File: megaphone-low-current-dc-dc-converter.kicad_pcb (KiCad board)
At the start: 4 copper layers, 38.7 x 60 mm, 53 parts, among them Q1 SI7272DP, Q3 2N7002, U2 AP63203WU, U3 ACS712-20A, U4 ACS712-20A, U5 MCP4018

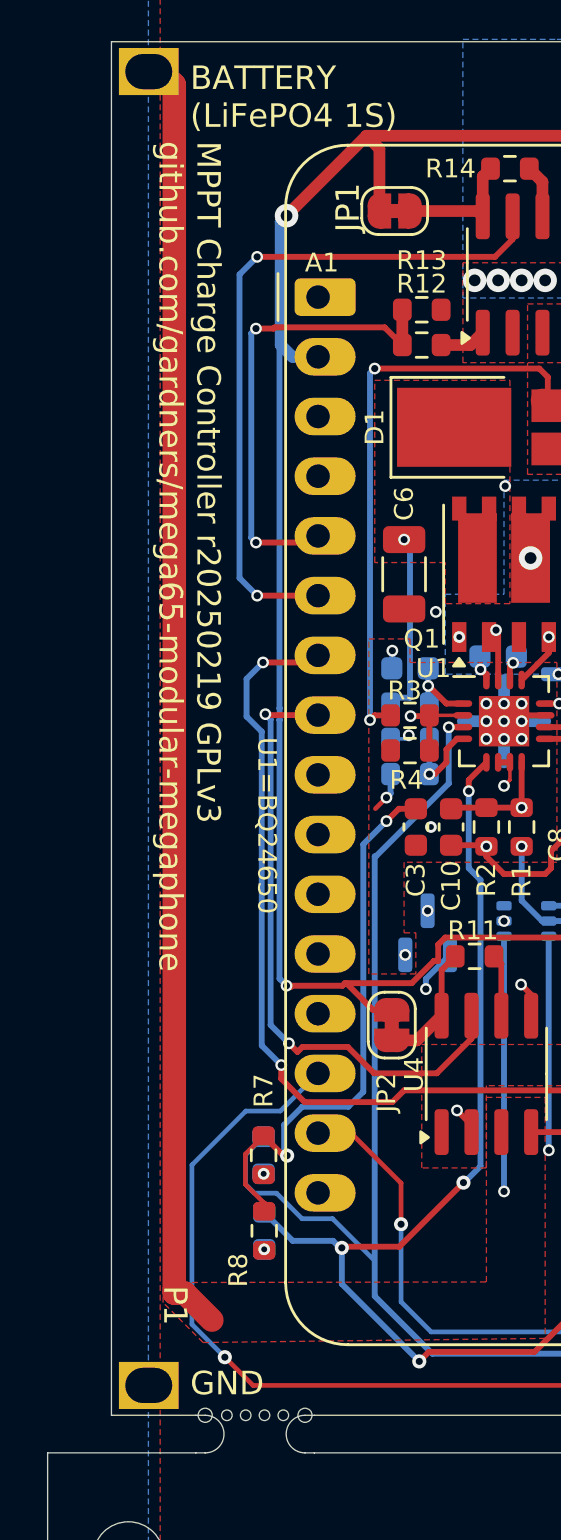
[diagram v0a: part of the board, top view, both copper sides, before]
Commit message: change all MPPT references in files to new project name
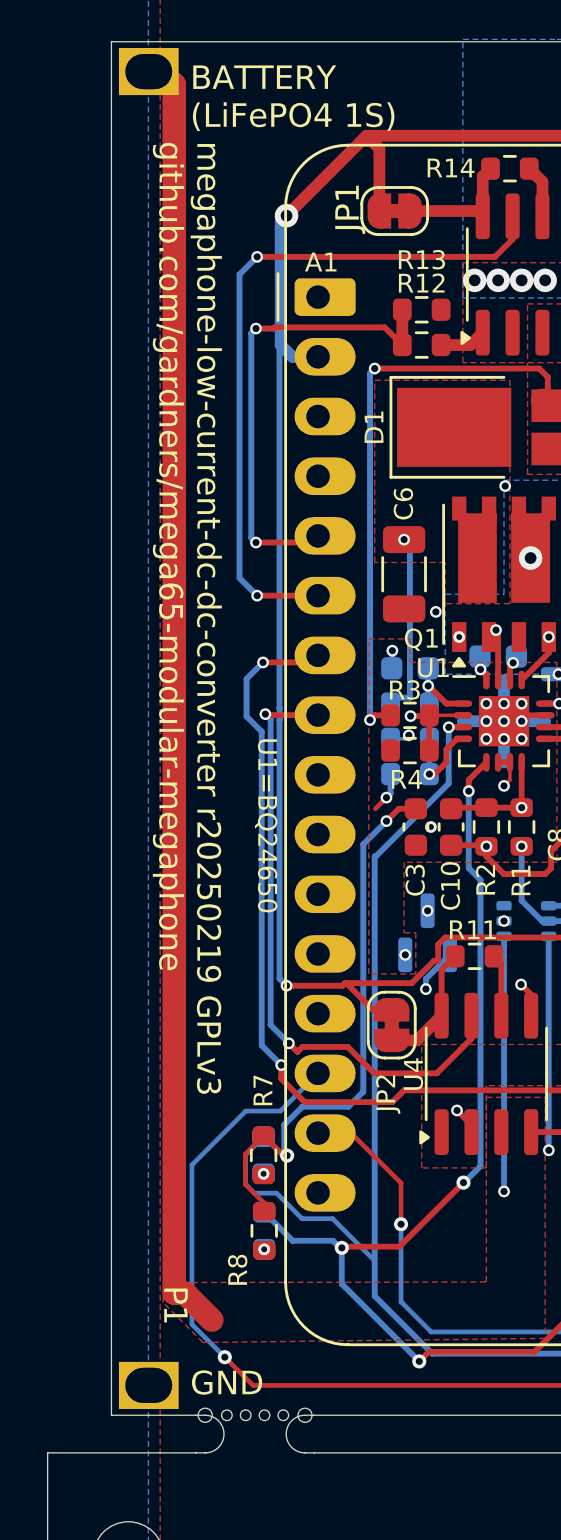
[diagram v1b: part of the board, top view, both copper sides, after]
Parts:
- L1: footprint MPPT Charge Controller Footprint Library:L_Vishay_6.9x6.5 -> megaphone-low-current-dc-dc-converter Footprint Library:L_Vishay_6.9x6.5
- U1: footprint MPPT Charge Controller Footprint Library:VQFN-16_EP_3.5x3.5_Pitch0.5mm -> megaphone-low-current-dc-dc-converter Footprint Library:VQFN-16_EP_3.5x3.5_Pitch0.5mm

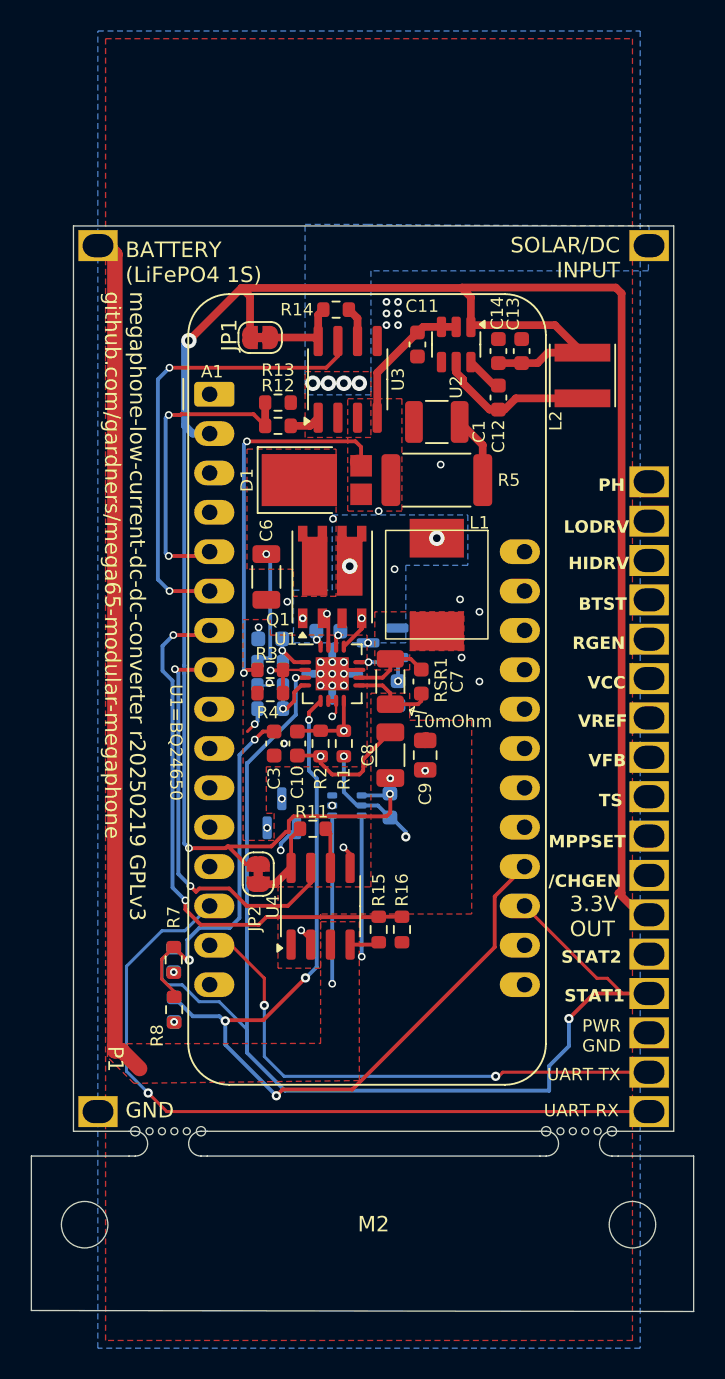
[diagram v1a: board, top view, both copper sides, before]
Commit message: prune out unnecessary part of schematic
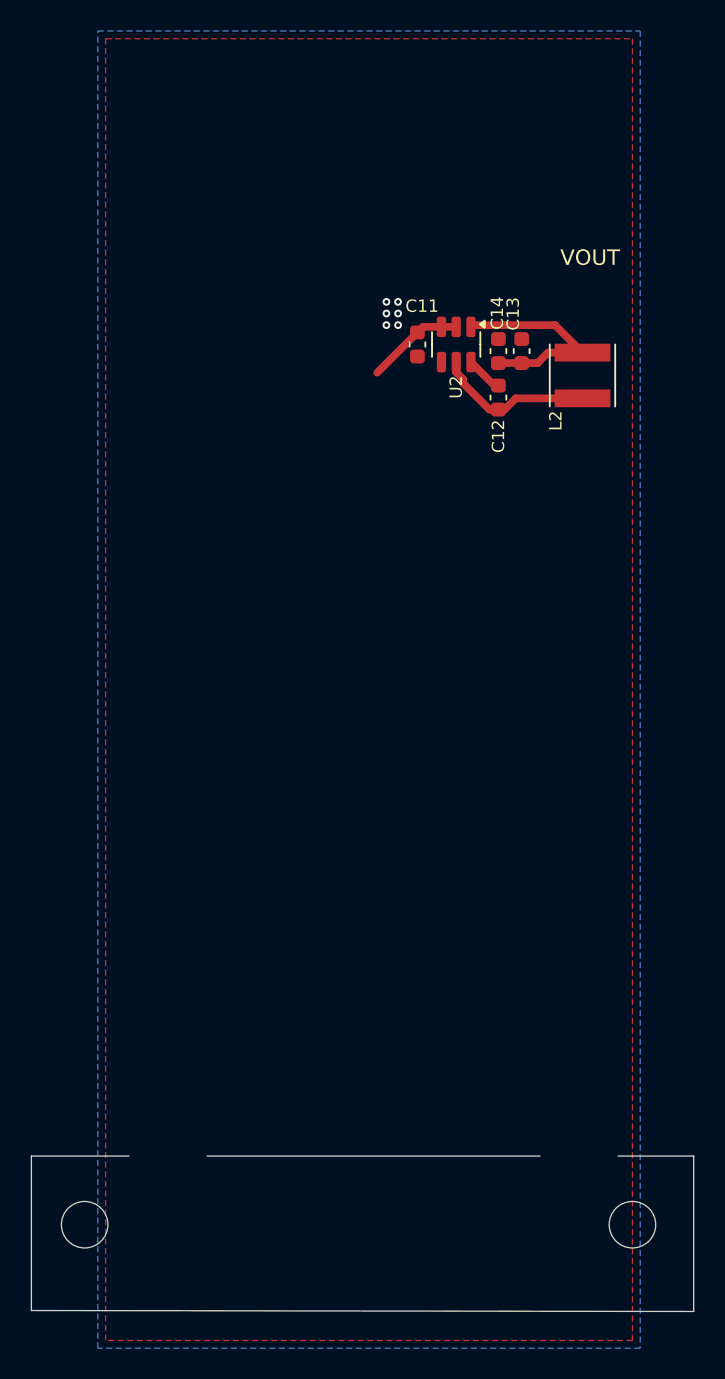
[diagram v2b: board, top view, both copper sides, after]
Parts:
- removed A1: Adafruit_Feather_HUZZAH32_ESP32, Module:Adafruit_Feather
- removed C1: 2.2uF, Capacitor_SMD:C_1210_3225Metric
- removed C10: 22pF, Capacitor_SMD:C_0603_1608Metric
- removed C15, C5, C7: 0.1uF, Capacitor_SMD:C_0603_1608Metric
- removed C2: C2=1uF, Capacitor_SMD:C_0603_1608Metric
- removed C3, C4: 1uF, Capacitor_SMD:C_0603_1608Metric
- removed C6, C8: 10uF, Capacitor_SMD:C_1206_3216Metric
- removed C9: 4.7uF, Capacitor_SMD:C_0805_2012Metric
- removed D1: PDS1040, Diode_SMD:D_PowerDI-5
- removed D2: BAT54C, Package_TO_SOT_SMD:SOT-23
- removed D3: RED, LED_SMD:LED_0603_1608Metric
- removed D4: GREEN, LED_SMD:LED_0603_1608Metric
- removed JP1, JP2: Jumper_2_Bridged, Jumper:SolderJumper-2_P1.3mm_Bridged_RoundedPad1.0x1.5mm
- removed L1: 10uH, megaphone-low-current-dc-dc-converter Footprint Library:L_Vishay_6.9x6.5
- removed M2: ~, MegaCastle:MegaCastle2x23-Module-I30.0x53.6-M80000307FFFC-PANEL-NIBBLE
- removed NT1, NT2, NT3, NT4: ~, NetTie:NetTie-2_SMD_Pad0.5mm
- removed Q1: SI7272DP, Package_SO:PowerPAK_SO-8_Dual
- removed Q3: 2N7002, Package_TO_SOT_SMD:SOT-23
- removed R1, R11, R14, R16: 100k, Resistor_SMD:R_0603_1608Metric
- removed R10: R10=30.1k, Resistor_SMD:R_0603_1608Metric
- removed R12, R15, R3: 499k, Resistor_SMD:R_0603_1608Metric
- removed R13: 36k, Resistor_SMD:R_0603_1608Metric
- removed R2: 140K, Resistor_SMD:R_0603_1608Metric
- removed R4: DNP, Resistor_SMD:R_0603_1608Metric
- removed R5: 2 Ohm, Resistor_SMD:R_2512_6332Metric
- removed R6: R6=10, Resistor_SMD:R_0603_1608Metric
- removed R7, R8: 100, Resistor_SMD:R_0603_1608Metric
- removed R9: R9=5.23k, Resistor_SMD:R_0603_1608Metric
- removed RSR1: 10mOhm, Resistor_SMD:R_1206_3216Metric
- removed U1: ~, megaphone-low-current-dc-dc-converter Footprint Library:VQFN-16_EP_3.5x3.5_Pitch0.5mm
- removed U3, U4: ACS712-20A, Package_SO:SOIC-8_3.9x4.9mm_P1.27mm
- removed U5: MCP4018, Package_TO_SOT_SMD:SOT-363_SC-70-6
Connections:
- net +3.3V renamed VOUT
- C11 pad 2: /VIN -> VBAT
- U2 pad 2: /VIN -> EN
- U2 pad 3: /VIN -> VBAT
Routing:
- net VOUT: track 146.3 -> 14.2 mm, vias 3 -> 0
- net /STAT1: track 79.1 -> 0.00 mm, vias 2 -> 0
- net /STAT2: track 69.8 -> 0.00 mm, vias 4 -> 0
- net VBAT_OUT: track 56.7 -> 0.00 mm
- net UART_RX: track 48.6 -> 0.00 mm, vias 1 -> 0
- net /VREF: track 48.5 -> 0.00 mm, vias 4 -> 0
- net /MPPSET: track 37.4 -> 0.00 mm, vias 3 -> 0
- net /Battery Voltage: track 35.7 -> 0.00 mm, vias 2 -> 0
- net UART_TX: track 34.9 -> 0.00 mm, vias 2 -> 0
- net /VCC: track 34.8 -> 0.00 mm, vias 4 -> 0
- net /VIN: track 34.3 -> 0.00 mm, vias 2 -> 0
- net PWR_GND: track 32.7 -> 0.00 mm, vias 14 -> 0
- net /TS: track 31.1 -> 0.00 mm, vias 2 -> 0
- net /HIDRV: track 30.0 -> 0.00 mm, vias 2 -> 0
- net /Solar Current: track 29.8 -> 0.00 mm, vias 2 -> 0
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- removed copper zone on B.Cu, net /Input
- removed copper zone on F.Cu, net /Input
- removed copper zone on B.Cu, net /PH
- removed copper zone on F.Cu, net /VIN
- removed copper zone on In1.Cu, net /VREF
- removed copper zone on F.Cu, net Net-(D1-K)
- removed copper zone on F.Cu, net Net-(U1-SRN)
- removed copper zone on F.Cu, net Net-(U1-SRP)
- removed copper zone on B.Cu, net PWR_GND
- removed copper zone on F.Cu, net PWR_GND
- removed copper zone on F.Cu, net VBAT_OUT
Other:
- board size 38.7 x 60 mm -> 42.7 x 10 mm
- board text added: "VOUT"
- board text removed: "${TITLE} r20250219 GPLv3 github.com/gardners/mega65-modular-megaphone"
- board text removed: "/CHGEN"
- board text removed: "3.3V OUT"
- board text removed: "BATTERY (LiFePO4 1S)"
- board text removed: "BTST"
- board text removed: "Charging"
- board text removed: "Done"
- board text removed: "GND"
- board text removed: "HIDRV"
- board text removed: "LODRV"
- board text removed: "MPPSET"
- board text removed: "P1"
- board text removed: "PH"
- board text removed: "PWR GND"
- board text removed: "RGEN"
- board text removed: "SOLAR/DC INPUT"
- board text removed: "STAT1"
- board text removed: "STAT2"
- board text removed: "TS"
- board text removed: "U1=BQ24650"
- board text removed: "UART RX"
- board text removed: "UART TX"
- board text removed: "VCC"
- board text removed: "VFB"
- board text removed: "VREF"

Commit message: finish adapting MPPT into simple low-current 3.3V DC:DC regulator
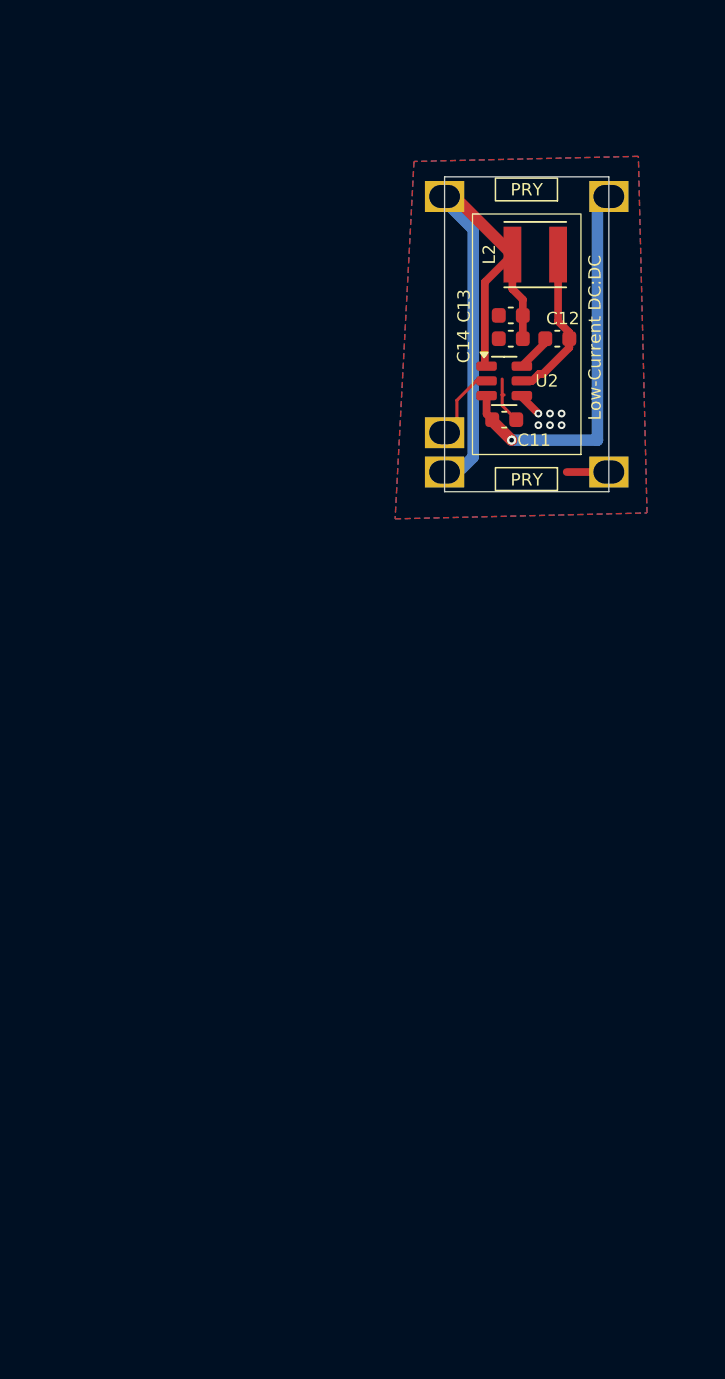
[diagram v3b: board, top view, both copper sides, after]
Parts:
- added M1: ~, MegaCastle:MegaCastle2x8-Module-I7.0x15.5-M8183, B.Cu at (120.2, 75.5)
- moved L2 8.38 mm to (120.7, 70.4), turned to 180 degrees
- moved C11 7.41 mm to (118.7, 81.0), turned to 180 degrees
- moved C12 5.37 mm to (122.2, 75.8), turned to 180 degrees
- moved U2 3.89 mm to (118.7, 78.5), turned to 0 degrees
- moved C13 2.40 mm to (119.2, 74.3), turned to 180 degrees
- moved C14 1.13 mm to (119.2, 75.8), turned to 180 degrees
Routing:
- net VOUT: track 14.2 -> 40.0 mm
- net VBAT: track 0.00 -> 25.1 mm, vias 0 -> 1
- net GND: track 0.00 -> 7.43 mm
- net (no net): track 6.32 -> 0.00 mm
- net EN: track 0.00 -> 4.85 mm
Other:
- board size 42.7 x 10 mm -> 10.6 x 20.3 mm
- copper layers 4 -> 2
- board text added: "3V3 OUT"
- board text added: "EN"
- board text added: "GND"
- board text added: "Low-Current DC:DC"
- board text added: "R20250222 github.com /gardners"
- board text added: "VBAT"
- board text added: "github.com/gardners"
- board text removed: "VOUT"

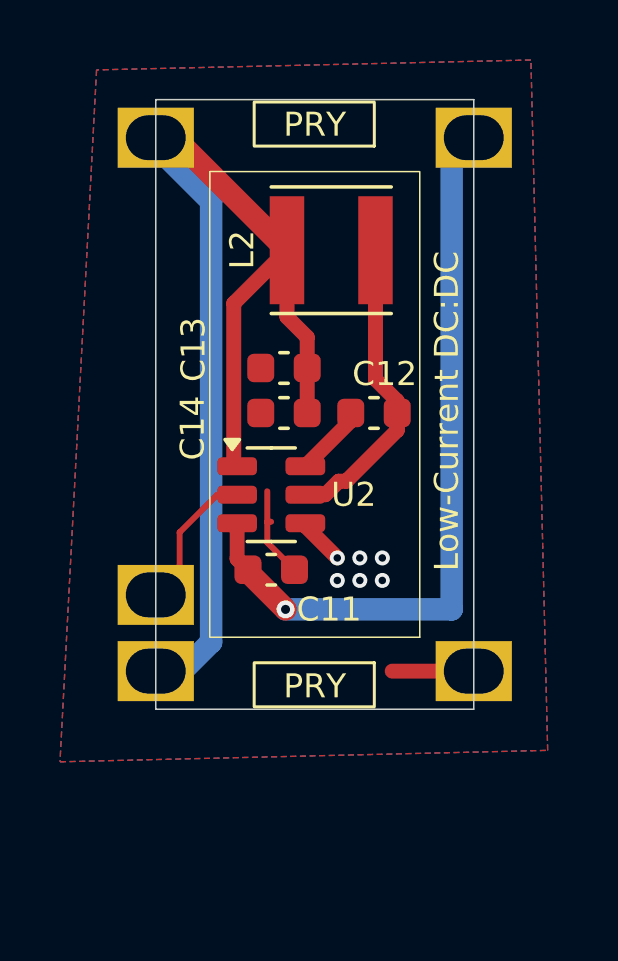
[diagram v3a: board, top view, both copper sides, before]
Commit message: use TPS631000 DC:DC converter
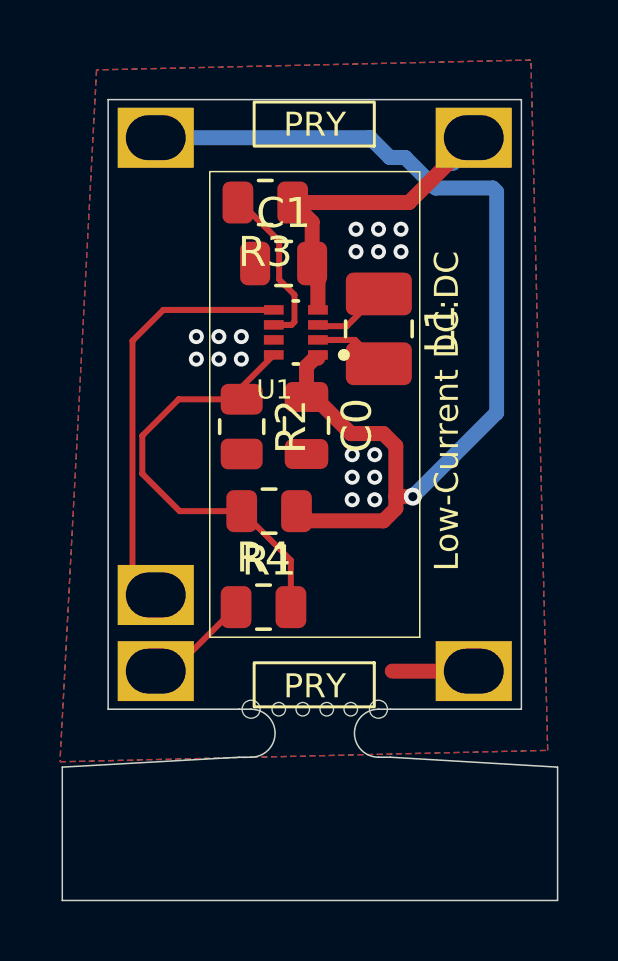
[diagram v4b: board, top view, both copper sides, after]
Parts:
- removed C12: 0.1uF, Capacitor_SMD:C_0603_1608Metric
- removed C13, C14: 22uF, Capacitor_SMD:C_0603_1608Metric
- removed U2: AP63203WU, Package_TO_SOT_SMD:TSOT-23-6
- added C0: 15uF, Capacitor_SMD:C_0805_2012Metric, F.Cu at (119.9, 76.2)
- added R1: 510K, Resistor_SMD:R_0805_2012Metric, F.Cu at (118.7, 79.1)
- added R2: 90.9K, Resistor_SMD:R_0805_2012Metric, F.Cu at (117.7, 76.3)
- added R3: 510K, Resistor_SMD:R_0805_2012Metric, F.Cu at (118.5, 68.8)
- added R4: 432K, Resistor_SMD:R_0805_2012Metric, F.Cu at (118.5, 82.3)
- added U1: TPS631000DRLR, megaphone-low-current-dc-dc-converter:SOT50P160X60-8N, F.Cu at (119.5, 73.1)
- C1: renamed from C11; value 10uF -> 47uF; footprint Capacitor_SMD:C_0603_1608Metric -> Capacitor_SMD:C_0805_2012Metric
- L1: renamed from L2; value 4.7uH -> 1uH; footprint Inductor_SMD:L_Vishay_IFSC-1515AH_4x4x1.8mm -> Inductor_SMD:L_1008_2520Metric_Pad1.43x2.20mm_HandSolder
- M1: footprint MegaCastle:MegaCastle2x8-Module-I7.0x15.5-M8183 -> MegaCastle:MegaCastle2x8-Module-I7.0x15.5-M8183-PANEL-NIBBLE
- moved C1 10.2 mm to (119.1, 70.8), turned to 0 degrees
- moved L1 3.06 mm to (122.3, 73.0), turned to -90 degrees
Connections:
- L1 pad 2: VOUT -> Net-(U1-LX2)
- M1 pad 16: VOUT -> SEL1V8
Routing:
- net Net-(U1-FB): track 0.00 -> 14.7 mm
- net VBAT: track 25.1 -> 11.9 mm, vias 1 -> 0
- net EN: track 4.85 -> 15.1 mm
- net Net-(U1-LX1): track 10.3 -> 2.49 mm
- net MODE: track 0.00 -> 5.54 mm
- net GND: track 7.43 -> 2.72 mm, vias 6 -> 18
- net SEL1V8: track 0.00 -> 4.44 mm
- net VOUT: track 40.0 -> 35.8 mm, vias 0 -> 1
- net Net-(U2-BST): track 2.40 -> 0.00 mm
- net Net-(U1-LX2): track 0.00 -> 2.36 mm
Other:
- board size 10.6 x 20.3 mm -> 13.8 x 21.9 mm

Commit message: finish PCB layout
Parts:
- removed M1: ~, MegaCastle:MegaCastle2x8-Module-I7.0x15.5-M8183-PANEL-NIBBLE
- added M2: ~, MegaCastle:MegaCastle2x8-Module-I7.0x15.5-M8187-PANEL-NIBBLE, B.Cu at (120.2, 75.6)
- U1: value TPS631000DRLR -> U1=TPS631000DRLR
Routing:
- net MODE: track 5.54 -> 21.8 mm
- net EN: track 15.1 -> 11.1 mm
- net Net-(U1-FB): track 14.7 -> 11.4 mm
- net VOUT: track 35.8 -> 38.6 mm
- net GND: track 2.72 -> 3.85 mm, vias 18 -> 22
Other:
- board text added: "1V8 SEL"
- board text added: "MODE"
- board text added: "R20250222"
- board text added: "Tie for 1V8"
- board text removed: "R20250222 github.com /gardners"
